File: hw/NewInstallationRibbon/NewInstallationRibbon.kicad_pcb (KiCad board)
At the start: 2 copper layers, 99.7 x 84.5 mm, 33 parts, among them J1 +5V, J10 D4, J12 LEFT, J13 RIGHT, J14 UP, J15 GND, J16 GND, J17 24 Pin Flex Connector, J18 DOWN, J19 R, J2 GND, J20 L, J21 START, J22 B2, J23 B1, J25 BRIGHT, J3 CLK, J4 SMS, J5 DW, J6 CL2, J7 D1, J8 D2, J9 D3

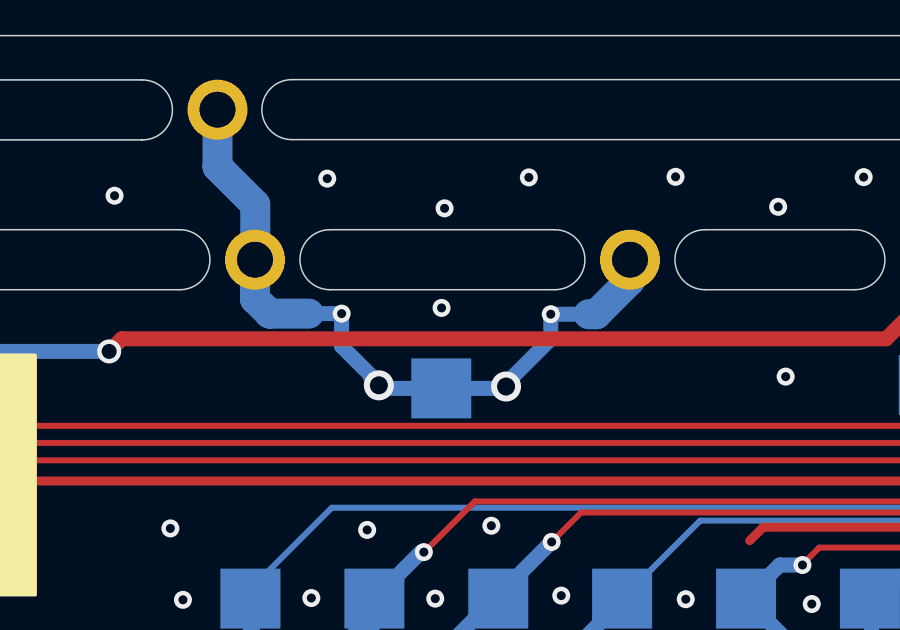
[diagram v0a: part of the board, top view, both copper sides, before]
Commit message: Fixed wrong GND pin on installation ribbon!
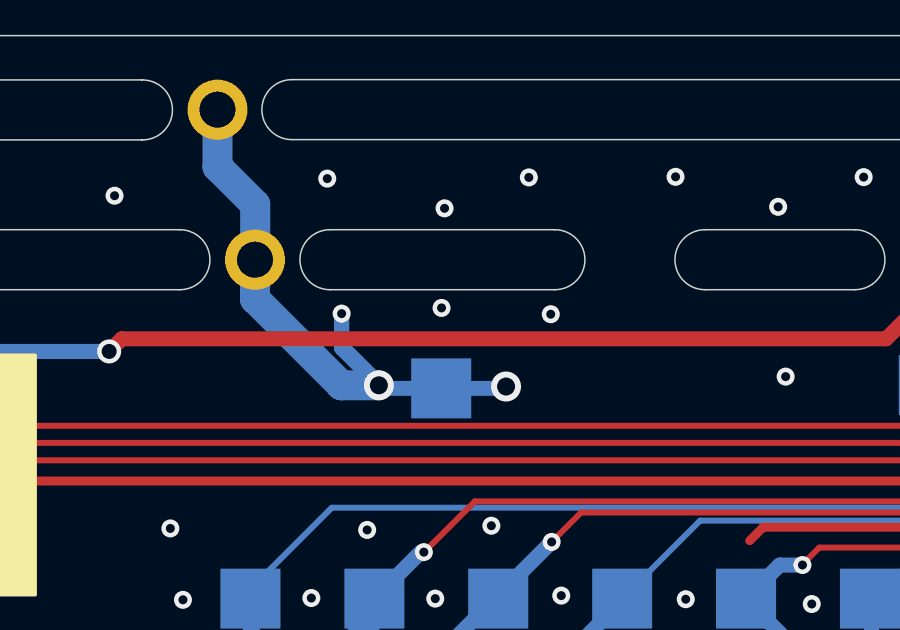
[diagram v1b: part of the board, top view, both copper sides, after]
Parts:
- removed J2: GND, gg_lcd:TestPoint_THTPad_D2.5mm_Drill1.2mm
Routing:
- net GND: track 605.9 -> 604.3 mm
